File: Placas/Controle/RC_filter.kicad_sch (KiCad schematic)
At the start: 2 parts

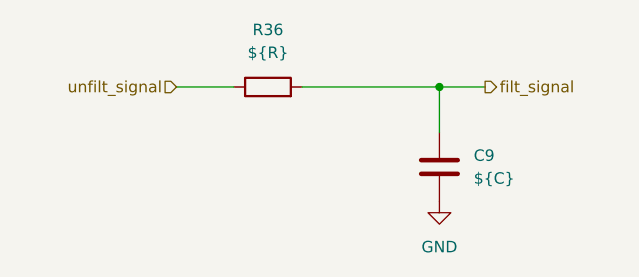
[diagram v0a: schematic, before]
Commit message: Adição de circuitos opcionais para PWM
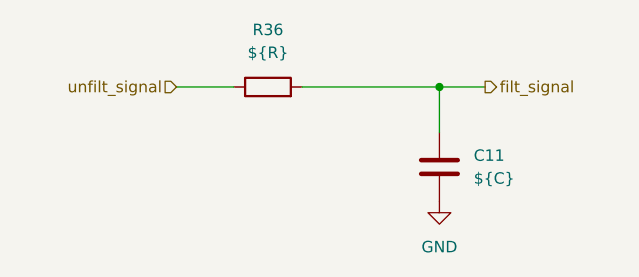
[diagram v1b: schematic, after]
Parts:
- renumbered C9 to C11
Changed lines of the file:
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@@
 		(dnp no)
 		(fields_autoplaced yes)
-		(property "Reference" "#PWR53"
+		(property "Reference" "#PWR55"
 			(at 107.95 110.49 0)
 			(effects
@@
 			(project "Controle"
 				(path "/01568b53-f202-4f02-9c1a-9c10c7610b4b/64ed1ee1-6201-4cd1-840c-b46b599d55ab/417fe5a9-3947-49d8-9a77-524f192b095c"
-					(reference "#PWR53")
+					(reference "#PWR55")
 					(unit 1)
 				)
 				(path "/01568b53-f202-4f02-9c1a-9c10c7610b4b/64ed1ee1-6201-4cd1-840c-b46b599d55ab/630f9e26-86d8-4dae-8668-563662ced3e2"
+					(reference "#PWR58")
+					(unit 1)
+				)
+				(path "/01568b53-f202-4f02-9c1a-9c10c7610b4b/64ed1ee1-6201-4cd1-840c-b46b599d55ab/76306f3e-e64d-46c5-8ffb-f9960fcc52ac"
+					(reference "#PWR59")
+					(unit 1)
+				)
+				(path "/01568b53-f202-4f02-9c1a-9c10c7610b4b/64ed1ee1-6201-4cd1-840c-b46b599d55ab/7d615356-24c6-4d5c-89f8-11ac3313c5e2"
+					(reference "#PWR54")
+					(unit 1)
+				)
+				(path "/01568b53-f202-4f02-9c1a-9c10c7610b4b/64ed1ee1-6201-4cd1-840c-b46b599d55ab/9c0bcb03-3eec-4e91-b96b-918272da8c10"
 					(reference "#PWR56")
 					(unit 1)
 				)
-				(path "/01568b53-f202-4f02-9c1a-9c10c7610b4b/64ed1ee1-6201-4cd1-840c-b46b599d55ab/76306f3e-e64d-46c5-8ffb-f9960fcc52ac"
+				(path "/01568b53-f202-4f02-9c1a-9c10c7610b4b/64ed1ee1-6201-4cd1-840c-b46b599d55ab/b66c4993-d833-4ac2-901f-a740ef9d69e4"
 					(reference "#PWR57")
-					(unit 1)
-				)
-				(path "/01568b53-f202-4f02-9c1a-9c10c7610b4b/64ed1ee1-6201-4cd1-840c-b46b599d55ab/7d615356-24c6-4d5c-89f8-11ac3313c5e2"
-					(reference "#PWR52")
-					(unit 1)
-				)
-				(path "/01568b53-f202-4f02-9c1a-9c10c7610b4b/64ed1ee1-6201-4cd1-840c-b46b599d55ab/9c0bcb03-3eec-4e91-b96b-918272da8c10"
-					(reference "#PWR54")
-					(unit 1)
-				)
-				(path "/01568b53-f202-4f02-9c1a-9c10c7610b4b/64ed1ee1-6201-4cd1-840c-b46b599d55ab/b66c4993-d833-4ac2-901f-a740ef9d69e4"
-					(reference "#PWR55")
 					(unit 1)
 				)
@@
 		(dnp no)
 		(fields_autoplaced yes)
-		(property "Reference" "C9"
+		(property "Reference" "C11"
 			(at 111.76 99.0599 0)
 			(effects
@@
 			(project "Controle"
 				(path "/01568b53-f202-4f02-9c1a-9c10c7610b4b/64ed1ee1-6201-4cd1-840c-b46b599d55ab/417fe5a9-3947-49d8-9a77-524f192b095c"
-					(reference "C9")
+					(reference "C11")
 					(unit 1)
 				)
 				(path "/01568b53-f202-4f02-9c1a-9c10c7610b4b/64ed1ee1-6201-4cd1-840c-b46b599d55ab/630f9e26-86d8-4dae-8668-563662ced3e2"
+					(reference "C14")
+					(unit 1)
+				)
+				(path "/01568b53-f202-4f02-9c1a-9c10c7610b4b/64ed1ee1-6201-4cd1-840c-b46b599d55ab/76306f3e-e64d-46c5-8ffb-f9960fcc52ac"
+					(reference "C15")
+					(unit 1)
+				)
+				(path "/01568b53-f202-4f02-9c1a-9c10c7610b4b/64ed1ee1-6201-4cd1-840c-b46b599d55ab/7d615356-24c6-4d5c-89f8-11ac3313c5e2"
+					(reference "C10")
+					(unit 1)
+				)
+				(path "/01568b53-f202-4f02-9c1a-9c10c7610b4b/64ed1ee1-6201-4cd1-840c-b46b599d55ab/9c0bcb03-3eec-4e91-b96b-918272da8c10"
 					(reference "C12")
 					(unit 1)
 				)
-				(path "/01568b53-f202-4f02-9c1a-9c10c7610b4b/64ed1ee1-6201-4cd1-840c-b46b599d55ab/76306f3e-e64d-46c5-8ffb-f9960fcc52ac"
+				(path "/01568b53-f202-4f02-9c1a-9c10c7610b4b/64ed1ee1-6201-4cd1-840c-b46b599d55ab/b66c4993-d833-4ac2-901f-a740ef9d69e4"
 					(reference "C13")
 					(unit 1)
 				)
-				(path "/01568b53-f202-4f02-9c1a-9c10c7610b4b/64ed1ee1-6201-4cd1-840c-b46b599d55ab/7d615356-24c6-4d5c-89f8-11ac3313c5e2"
-					(reference "C8")
-					(unit 1)
-				)
-				(path "/01568b53-f202-4f02-9c1a-9c10c7610b4b/64ed1ee1-6201-4cd1-840c-b46b599d55ab/9c0bcb03-3eec-4e91-b96b-918272da8c10"
-					(reference "C10")
-					(unit 1)
-				)
-				(path "/01568b53-f202-4f02-9c1a-9c10c7610b4b/64ed1ee1-6201-4cd1-840c-b46b599d55ab/b66c4993-d833-4ac2-901f-a740ef9d69e4"
-					(reference "C11")
-					(unit 1)
-				)

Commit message: Modificações nas duas placas, adição de furos para montagem, melhora na posição dos micros e conectores para comunicação SPI
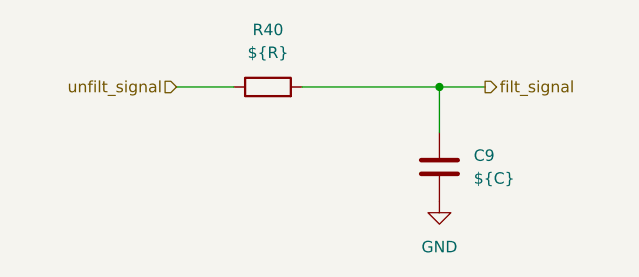
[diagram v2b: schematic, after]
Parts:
- C9: renamed from C11; footprint Capacitor_THT:C_Disc_D8.0mm_W5.0mm_P7.50mm -> Capacitor_SMD:C_0805_2012Metric_Pad1.18x1.45mm_HandSolder
- R40: renamed from R36; footprint Resistor_THT:R_Axial_DIN0207_L6.3mm_D2.5mm_P7.62mm_Horizontal -> Resistor_SMD:R_0805_2012Metric_Pad1.20x1.40mm_HandSolder
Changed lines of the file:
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@@
 		(dnp no)
 		(fields_autoplaced yes)
-		(property "Reference" "#PWR55"
+		(property "Reference" "#PWR61"
 			(at 107.95 110.49 0)
 			(effects
@@
 			(project "Controle"
 				(path "/01568b53-f202-4f02-9c1a-9c10c7610b4b/64ed1ee1-6201-4cd1-840c-b46b599d55ab/417fe5a9-3947-49d8-9a77-524f192b095c"
-					(reference "#PWR55")
+					(reference "#PWR61")
 					(unit 1)
 				)
 				(path "/01568b53-f202-4f02-9c1a-9c10c7610b4b/64ed1ee1-6201-4cd1-840c-b46b599d55ab/630f9e26-86d8-4dae-8668-563662ced3e2"
-					(reference "#PWR58")
+					(reference "#PWR64")
 					(unit 1)
 				)
 				(path "/01568b53-f202-4f02-9c1a-9c10c7610b4b/64ed1ee1-6201-4cd1-840c-b46b599d55ab/76306f3e-e64d-46c5-8ffb-f9960fcc52ac"
-					(reference "#PWR59")
+					(reference "#PWR65")
 					(unit 1)
 				)
 				(path "/01568b53-f202-4f02-9c1a-9c10c7610b4b/64ed1ee1-6201-4cd1-840c-b46b599d55ab/7d615356-24c6-4d5c-89f8-11ac3313c5e2"
-					(reference "#PWR54")
+					(reference "#PWR60")
 					(unit 1)
 				)
 				(path "/01568b53-f202-4f02-9c1a-9c10c7610b4b/64ed1ee1-6201-4cd1-840c-b46b599d55ab/9c0bcb03-3eec-4e91-b96b-918272da8c10"
-					(reference "#PWR56")
+					(reference "#PWR62")
 					(unit 1)
 				)
 				(path "/01568b53-f202-4f02-9c1a-9c10c7610b4b/64ed1ee1-6201-4cd1-840c-b46b599d55ab/b66c4993-d833-4ac2-901f-a740ef9d69e4"
-					(reference "#PWR57")
+					(reference "#PWR63")
 					(unit 1)
 				)
@@
 		(dnp no)
 		(fields_autoplaced yes)
-		(property "Reference" "R36"
+		(property "Reference" "R40"
 			(at 88.9 85.09 90)
 			(effects
@@
 			)
 		)
-		(property "Footprint" "Resistor_THT:R_Axial_DIN0207_L6.3mm_D2.5mm_P7.62mm_Horizontal"
+		(property "Footprint" "Resistor_SMD:R_0805_2012Metric_Pad1.20x1.40mm_HandSolder"
 			(at 88.9 93.218 90)
 			(effects
@@
 			(project "Controle"
 				(path "/01568b53-f202-4f02-9c1a-9c10c7610b4b/64ed1ee1-6201-4cd1-840c-b46b599d55ab/417fe5a9-3947-49d8-9a77-524f192b095c"
-					(reference "R36")
+					(reference "R40")
 					(unit 1)
 				)
 				(path "/01568b53-f202-4f02-9c1a-9c10c7610b4b/64ed1ee1-6201-4cd1-840c-b46b599d55ab/630f9e26-86d8-4dae-8668-563662ced3e2"
+					(reference "R43")
+					(unit 1)
+				)
+				(path "/01568b53-f202-4f02-9c1a-9c10c7610b4b/64ed1ee1-6201-4cd1-840c-b46b599d55ab/76306f3e-e64d-46c5-8ffb-f9960fcc52ac"
+					(reference "R44")
+					(unit 1)
+				)
+				(path "/01568b53-f202-4f02-9c1a-9c10c7610b4b/64ed1ee1-6201-4cd1-840c-b46b599d55ab/7d615356-24c6-4d5c-89f8-11ac3313c5e2"
 					(reference "R39")
 					(unit 1)
 				)
-				(path "/01568b53-f202-4f02-9c1a-9c10c7610b4b/64ed1ee1-6201-4cd1-840c-b46b599d55ab/76306f3e-e64d-46c5-8ffb-f9960fcc52ac"
-					(reference "R40")
-					(unit 1)
-				)
-				(path "/01568b53-f202-4f02-9c1a-9c10c7610b4b/64ed1ee1-6201-4cd1-840c-b46b599d55ab/7d615356-24c6-4d5c-89f8-11ac3313c5e2"
-					(reference "R35")
-					(unit 1)
-				)
 				(path "/01568b53-f202-4f02-9c1a-9c10c7610b4b/64ed1ee1-6201-4cd1-840c-b46b599d55ab/9c0bcb03-3eec-4e91-b96b-918272da8c10"
-					(reference "R37")
+					(reference "R41")
 					(unit 1)
 				)
 				(path "/01568b53-f202-4f02-9c1a-9c10c7610b4b/64ed1ee1-6201-4cd1-840c-b46b599d55ab/b66c4993-d833-4ac2-901f-a740ef9d69e4"
-					(reference "R38")
+					(reference "R42")
 					(unit 1)
 				)
@@
 		(dnp no)
 		(fields_autoplaced yes)
-		(property "Reference" "C11"
+		(property "Reference" "C9"
 			(at 111.76 99.0599 0)
 			(effects
@@
 			)
 		)
-		(property "Footprint" "Capacitor_THT:C_Disc_D8.0mm_W5.0mm_P7.50mm"
+		(property "Footprint" "Capacitor_SMD:C_0805_2012Metric_Pad1.18x1.45mm_HandSolder"
 			(at 108.9152 104.14 0)
 			(effects
@@
 			(project "Controle"
 				(path "/01568b53-f202-4f02-9c1a-9c10c7610b4b/64ed1ee1-6201-4cd1-840c-b46b599d55ab/417fe5a9-3947-49d8-9a77-524f192b095c"
+					(reference "C9")
+					(unit 1)
+				)
+				(path "/01568b53-f202-4f02-9c1a-9c10c7610b4b/64ed1ee1-6201-4cd1-840c-b46b599d55ab/630f9e26-86d8-4dae-8668-563662ced3e2"
+					(reference "C12")
+					(unit 1)
+				)
+				(path "/01568b53-f202-4f02-9c1a-9c10c7610b4b/64ed1ee1-6201-4cd1-840c-b46b599d55ab/76306f3e-e64d-46c5-8ffb-f9960fcc52ac"
+					(reference "C13")
+					(unit 1)
+				)
+				(path "/01568b53-f202-4f02-9c1a-9c10c7610b4b/64ed1ee1-6201-4cd1-840c-b46b599d55ab/7d615356-24c6-4d5c-89f8-11ac3313c5e2"
+					(reference "C8")
+					(unit 1)
+				)
+				(path "/01568b53-f202-4f02-9c1a-9c10c7610b4b/64ed1ee1-6201-4cd1-840c-b46b599d55ab/9c0bcb03-3eec-4e91-b96b-918272da8c10"
+					(reference "C10")
+					(unit 1)
+				)
+				(path "/01568b53-f202-4f02-9c1a-9c10c7610b4b/64ed1ee1-6201-4cd1-840c-b46b599d55ab/b66c4993-d833-4ac2-901f-a740ef9d69e4"
 					(reference "C11")
 					(unit 1)
 				)
-				(path "/01568b53-f202-4f02-9c1a-9c10c7610b4b/64ed1ee1-6201-4cd1-840c-b46b599d55ab/630f9e26-86d8-4dae-8668-563662ced3e2"
-					(reference "C14")
-					(unit 1)
-				)
-				(path "/01568b53-f202-4f02-9c1a-9c10c7610b4b/64ed1ee1-6201-4cd1-840c-b46b599d55ab/76306f3e-e64d-46c5-8ffb-f9960fcc52ac"
-					(reference "C15")
-					(unit 1)
-				)
-				(path "/01568b53-f202-4f02-9c1a-9c10c7610b4b/64ed1ee1-6201-4cd1-840c-b46b599d55ab/7d615356-24c6-4d5c-89f8-11ac3313c5e2"
-					(reference "C10")
-					(unit 1)
-				)
-				(path "/01568b53-f202-4f02-9c1a-9c10c7610b4b/64ed1ee1-6201-4cd1-840c-b46b599d55ab/9c0bcb03-3eec-4e91-b96b-918272da8c10"
-					(reference "C12")
-					(unit 1)
-				)
-				(path "/01568b53-f202-4f02-9c1a-9c10c7610b4b/64ed1ee1-6201-4cd1-840c-b46b599d55ab/b66c4993-d833-4ac2-901f-a740ef9d69e4"
-					(reference "C13")
-					(unit 1)
-				)

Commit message: Mudanças no firmware e calibração da tensão de entrada e saída
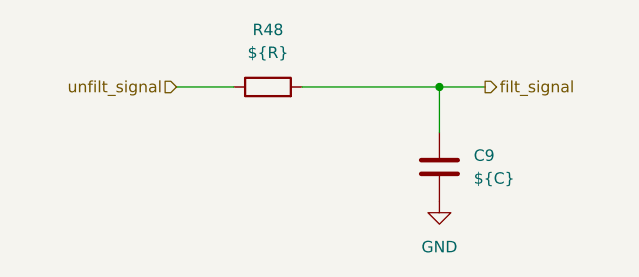
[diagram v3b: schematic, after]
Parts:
- renumbered R40 to R48
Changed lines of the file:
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@@
 		(dnp no)
 		(fields_autoplaced yes)
-		(property "Reference" "#PWR61"
+		(property "Reference" "#PWR68"
 			(at 107.95 110.49 0)
 			(effects
@@
 			(project "Controle"
 				(path "/01568b53-f202-4f02-9c1a-9c10c7610b4b/64ed1ee1-6201-4cd1-840c-b46b599d55ab/417fe5a9-3947-49d8-9a77-524f192b095c"
-					(reference "#PWR61")
+					(reference "#PWR68")
 					(unit 1)
 				)
 				(path "/01568b53-f202-4f02-9c1a-9c10c7610b4b/64ed1ee1-6201-4cd1-840c-b46b599d55ab/630f9e26-86d8-4dae-8668-563662ced3e2"
-					(reference "#PWR64")
+					(reference "#PWR71")
 					(unit 1)
 				)
 				(path "/01568b53-f202-4f02-9c1a-9c10c7610b4b/64ed1ee1-6201-4cd1-840c-b46b599d55ab/76306f3e-e64d-46c5-8ffb-f9960fcc52ac"
-					(reference "#PWR65")
+					(reference "#PWR72")
 					(unit 1)
 				)
 				(path "/01568b53-f202-4f02-9c1a-9c10c7610b4b/64ed1ee1-6201-4cd1-840c-b46b599d55ab/7d615356-24c6-4d5c-89f8-11ac3313c5e2"
-					(reference "#PWR60")
+					(reference "#PWR67")
 					(unit 1)
 				)
 				(path "/01568b53-f202-4f02-9c1a-9c10c7610b4b/64ed1ee1-6201-4cd1-840c-b46b599d55ab/9c0bcb03-3eec-4e91-b96b-918272da8c10"
-					(reference "#PWR62")
+					(reference "#PWR69")
 					(unit 1)
 				)
 				(path "/01568b53-f202-4f02-9c1a-9c10c7610b4b/64ed1ee1-6201-4cd1-840c-b46b599d55ab/b66c4993-d833-4ac2-901f-a740ef9d69e4"
-					(reference "#PWR63")
+					(reference "#PWR70")
 					(unit 1)
 				)
@@
 		(dnp no)
 		(fields_autoplaced yes)
-		(property "Reference" "R40"
+		(property "Reference" "R48"
 			(at 88.9 85.09 90)
 			(effects
@@
 			(project "Controle"
 				(path "/01568b53-f202-4f02-9c1a-9c10c7610b4b/64ed1ee1-6201-4cd1-840c-b46b599d55ab/417fe5a9-3947-49d8-9a77-524f192b095c"
-					(reference "R40")
+					(reference "R48")
 					(unit 1)
 				)
 				(path "/01568b53-f202-4f02-9c1a-9c10c7610b4b/64ed1ee1-6201-4cd1-840c-b46b599d55ab/630f9e26-86d8-4dae-8668-563662ced3e2"
-					(reference "R43")
+					(reference "R51")
 					(unit 1)
 				)
 				(path "/01568b53-f202-4f02-9c1a-9c10c7610b4b/64ed1ee1-6201-4cd1-840c-b46b599d55ab/76306f3e-e64d-46c5-8ffb-f9960fcc52ac"
-					(reference "R44")
+					(reference "R52")
 					(unit 1)
 				)
 				(path "/01568b53-f202-4f02-9c1a-9c10c7610b4b/64ed1ee1-6201-4cd1-840c-b46b599d55ab/7d615356-24c6-4d5c-89f8-11ac3313c5e2"
-					(reference "R39")
+					(reference "R47")
 					(unit 1)
 				)
 				(path "/01568b53-f202-4f02-9c1a-9c10c7610b4b/64ed1ee1-6201-4cd1-840c-b46b599d55ab/9c0bcb03-3eec-4e91-b96b-918272da8c10"
-					(reference "R41")
+					(reference "R49")
 					(unit 1)
 				)
 				(path "/01568b53-f202-4f02-9c1a-9c10c7610b4b/64ed1ee1-6201-4cd1-840c-b46b599d55ab/b66c4993-d833-4ac2-901f-a740ef9d69e4"
-					(reference "R42")
+					(reference "R50")
 					(unit 1)
 				)
